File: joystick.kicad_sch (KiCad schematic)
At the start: 17 parts, among them J3 DB9_Male, J4 DB9_Male, U5 TXB0106PWR, U6 MCP23S17

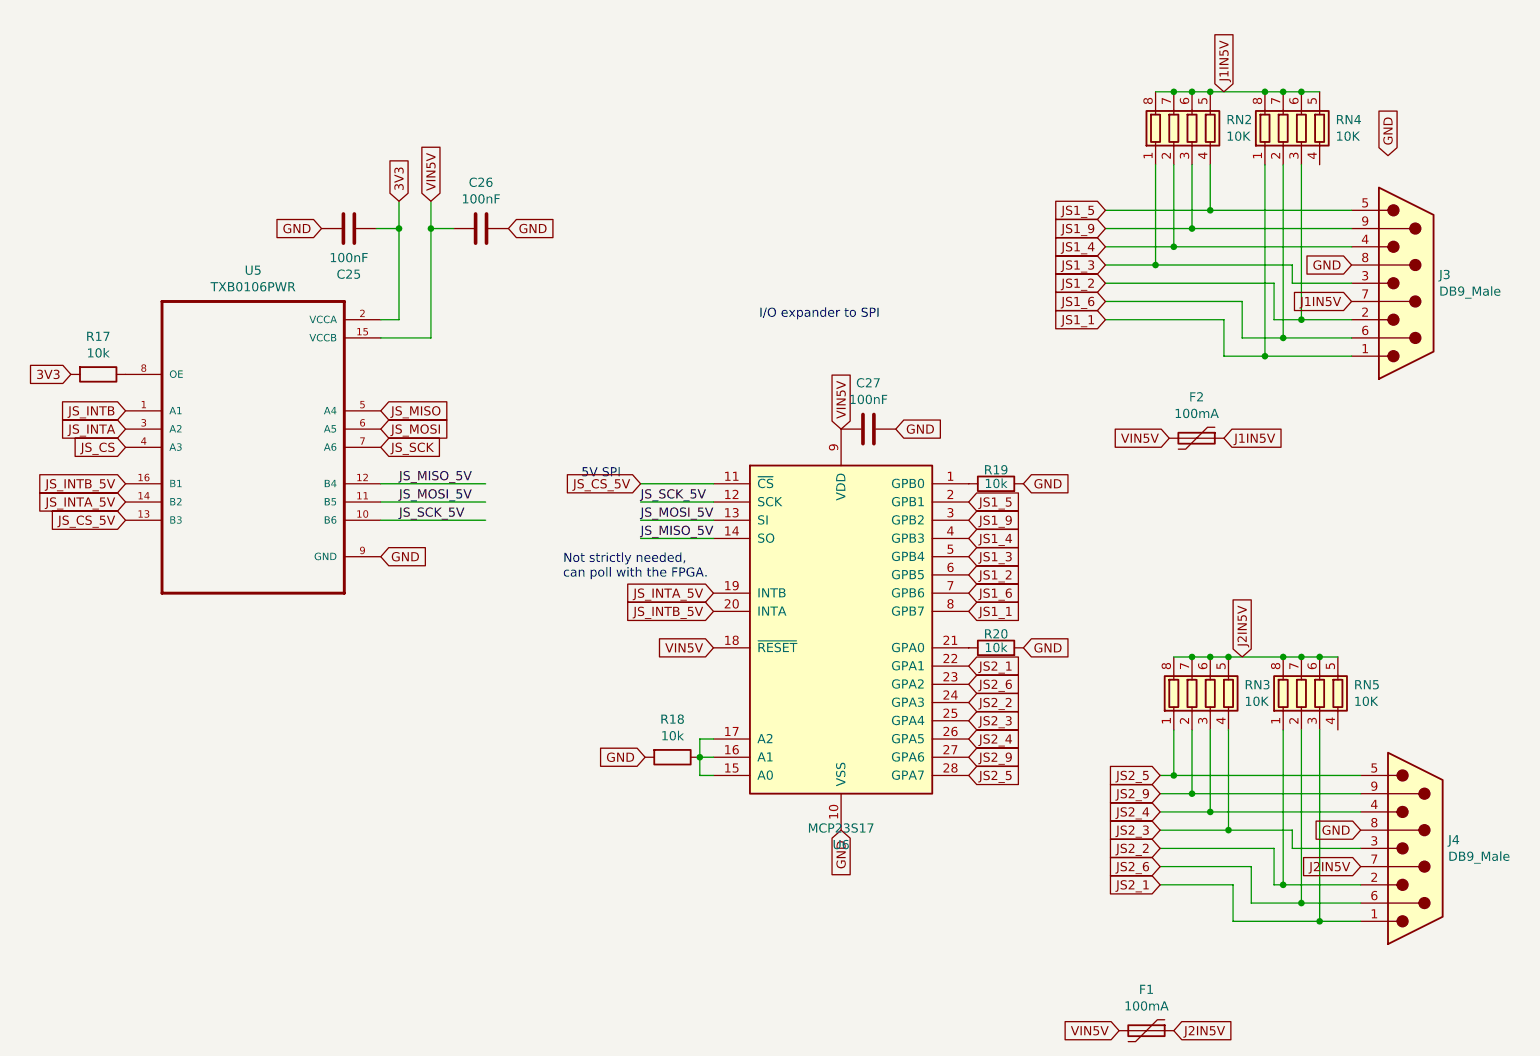
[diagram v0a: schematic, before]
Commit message: Prod version of OpenAARS 5.0 design.
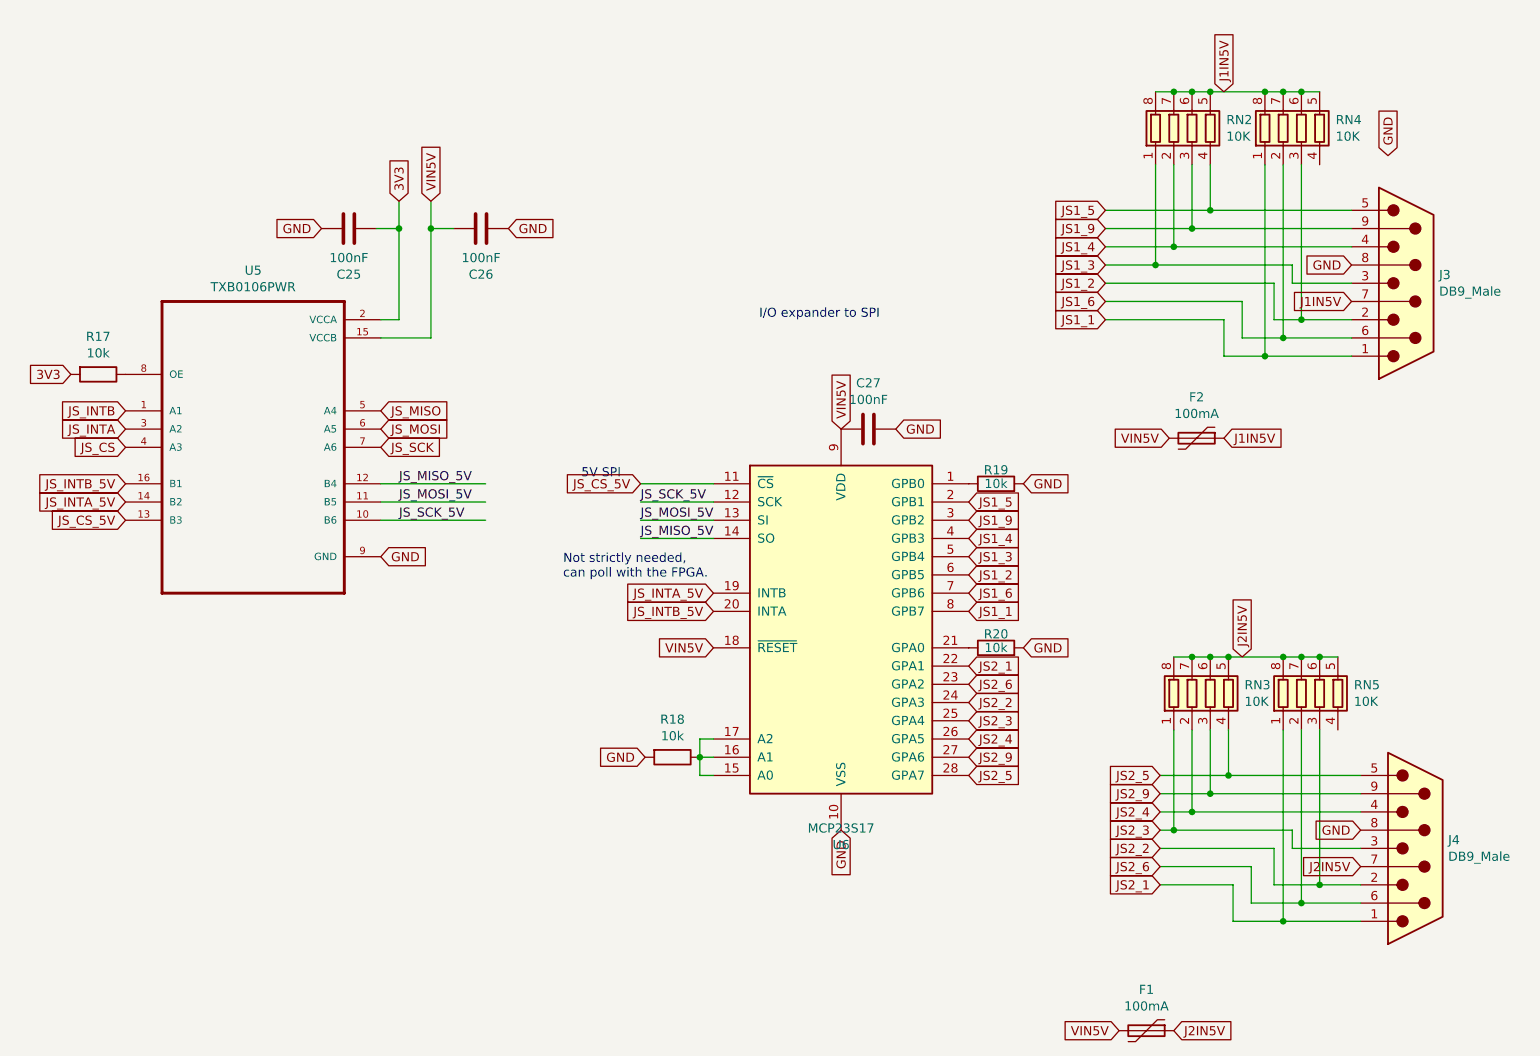
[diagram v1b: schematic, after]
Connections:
- net GND: now also C26.2; no longer C26.1
- net JS2_1: now also RN5.1 (R1.1); no longer RN5.3 (R3.1)
- net JS2_2: now also RN5.3 (R3.1); no longer RN5.1 (R1.1)
- net JS2_3: now also RN3.1 (R1.1); no longer RN3.4 (R4.1)
- net JS2_4: now also RN3.2 (R2.1); no longer RN3.3 (R3.1)
- net JS2_5: now also RN3.4 (R4.1); no longer RN3.1 (R1.1)
- net JS2_9: now also RN3.3 (R3.1); no longer RN3.2 (R2.1)
- net VIN5V: now also C26.1; no longer C26.2
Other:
- moved on the sheet: C26
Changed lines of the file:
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@@
   (junction (at 193.675 64.77) (diameter 0) (color 0 0 0 0)
   )
-  (junction (at 201.295 143.51) (diameter 0) (color 0 0 0 0)
-  )
   (junction (at 196.215 106.68) (diameter 0) (color 0 0 0 0)
   )
   (junction (at 201.295 106.68) (diameter 0) (color 0 0 0 0)
   )
-  (junction (at 180.975 123.19) (diameter 0) (color 0 0 0 0)
-  )
-  (junction (at 186.055 128.27) (diameter 0) (color 0 0 0 0)
-  )
   (junction (at 193.675 27.94) (diameter 0) (color 0 0 0 0)
   )
+  (junction (at 196.215 143.51) (diameter 0) (color 0 0 0 0)
+  )
   (junction (at 198.755 59.69) (diameter 0) (color 0 0 0 0)
   )
-  (junction (at 183.515 125.73) (diameter 0) (color 0 0 0 0)
-  )
   (junction (at 188.595 106.68) (diameter 0) (color 0 0 0 0)
   )
-  (junction (at 196.215 138.43) (diameter 0) (color 0 0 0 0)
-  )
   (junction (at 180.975 49.53) (diameter 0) (color 0 0 0 0)
   )
   (junction (at 180.975 27.94) (diameter 0) (color 0 0 0 0)
   )
+  (junction (at 186.055 125.73) (diameter 0) (color 0 0 0 0)
+  )
   (junction (at 73.025 46.99) (diameter 0) (color 0 0 0 0)
   )
+  (junction (at 188.595 123.19) (diameter 0) (color 0 0 0 0)
+  )
   (junction (at 186.055 44.45) (diameter 0) (color 0 0 0 0)
   )
@@
   (junction (at 186.055 106.68) (diameter 0) (color 0 0 0 0)
   )
+  (junction (at 201.295 138.43) (diameter 0) (color 0 0 0 0)
+  )
   (junction (at 196.215 62.23) (diameter 0) (color 0 0 0 0)
   )
@@
   (junction (at 183.515 106.68) (diameter 0) (color 0 0 0 0)
   )
+  (junction (at 183.515 128.27) (diameter 0) (color 0 0 0 0)
+  )
   (junction (at 198.755 27.94) (diameter 0) (color 0 0 0 0)
   )
@@
   (junction (at 183.515 27.94) (diameter 0) (color 0 0 0 0)
   )
-  (junction (at 188.595 130.81) (diameter 0) (color 0 0 0 0)
+  (junction (at 180.975 130.81) (diameter 0) (color 0 0 0 0)
   )
   (junction (at 114.935 120.65) (diameter 0) (color 0 0 0 0)
@@
     (stroke (width 0) (type default))
   )
-  (wire (pts (xy 188.595 130.81) (xy 197.485 130.81))
+  (wire (pts (xy 180.975 130.81) (xy 197.485 130.81))
     (stroke (width 0) (type default))
   )
@@
     (stroke (width 0) (type default))
   )
-  (wire (pts (xy 201.295 116.84) (xy 201.295 143.51))
+  (wire (pts (xy 196.215 116.84) (xy 196.215 143.51))
     (stroke (width 0) (type default))
   )
@@
     (stroke (width 0) (type default))
   )
-  (wire (pts (xy 180.975 116.84) (xy 180.975 123.19))
+  (wire (pts (xy 188.595 116.84) (xy 188.595 123.19))
     (stroke (width 0) (type default))
   )
@@
     (stroke (width 0) (type default))
   )
-  (wire (pts (xy 188.595 116.84) (xy 188.595 130.81))
-    (stroke (width 0) (type default))
-  )
   (wire (pts (xy 183.515 106.68) (xy 186.055 106.68))
     (stroke (width 0) (type default))
@@
     (stroke (width 0) (type default))
   )
-  (wire (pts (xy 194.945 138.43) (xy 196.215 138.43))
-    (stroke (width 0) (type default))
-  )
-  (wire (pts (xy 189.23 143.51) (xy 201.295 143.51))
-    (stroke (width 0) (type default))
-  )
-  (wire (pts (xy 179.07 123.19) (xy 180.975 123.19))
+  (wire (pts (xy 194.945 138.43) (xy 201.295 138.43))
+    (stroke (width 0) (type default))
+  )
+  (wire (pts (xy 189.23 143.51) (xy 196.215 143.51))
+    (stroke (width 0) (type default))
+  )
+  (wire (pts (xy 179.07 123.19) (xy 188.595 123.19))
     (stroke (width 0) (type default))
   )
@@
     (stroke (width 0) (type default))
   )
-  (wire (pts (xy 186.055 128.27) (xy 207.01 128.27))
-    (stroke (width 0) (type default))
-  )
   (wire (pts (xy 198.755 116.84) (xy 198.755 140.97))
     (stroke (width 0) (type default))
@@
     (stroke (width 0) (type default))
   )
-  (wire (pts (xy 179.07 128.27) (xy 186.055 128.27))
+  (wire (pts (xy 179.07 128.27) (xy 183.515 128.27))
     (stroke (width 0) (type default))
   )
@@
     (stroke (width 0) (type default))
   )
+  (wire (pts (xy 180.975 116.84) (xy 180.975 130.81))
+    (stroke (width 0) (type default))
+  )
+  (wire (pts (xy 186.055 125.73) (xy 207.01 125.73))
+    (stroke (width 0) (type default))
+  )
   (wire (pts (xy 171.45 57.15) (xy 190.5 57.15))
     (stroke (width 0) (type default))
@@
     (stroke (width 0) (type default))
   )
-  (wire (pts (xy 186.055 116.84) (xy 186.055 128.27))
-    (stroke (width 0) (type default))
-  )
   (wire (pts (xy 183.515 27.94) (xy 186.055 27.94))
     (stroke (width 0) (type default))
@@
     (stroke (width 0) (type default))
   )
-  (wire (pts (xy 179.07 130.81) (xy 188.595 130.81))
-    (stroke (width 0) (type default))
-  )
-  (wire (pts (xy 179.07 125.73) (xy 183.515 125.73))
+  (wire (pts (xy 179.07 130.81) (xy 180.975 130.81))
     (stroke (width 0) (type default))
   )
@@
     (stroke (width 0) (type default))
   )
-  (wire (pts (xy 201.295 143.51) (xy 207.01 143.51))
+  (wire (pts (xy 183.515 128.27) (xy 207.01 128.27))
     (stroke (width 0) (type default))
   )
@@
     (stroke (width 0) (type default))
   )
-  (wire (pts (xy 180.975 123.19) (xy 207.01 123.19))
-    (stroke (width 0) (type default))
-  )
   (wire (pts (xy 196.215 106.68) (xy 198.755 106.68))
     (stroke (width 0) (type default))
@@
     (stroke (width 0) (type default))
   )
-  (wire (pts (xy 196.215 116.84) (xy 196.215 138.43))
+  (wire (pts (xy 201.295 138.43) (xy 207.01 138.43))
+    (stroke (width 0) (type default))
+  )
+  (wire (pts (xy 183.515 116.84) (xy 183.515 128.27))
+    (stroke (width 0) (type default))
+  )
+  (wire (pts (xy 201.295 116.84) (xy 201.295 138.43))
     (stroke (width 0) (type default))
   )
@@
     (stroke (width 0) (type default))
   )
-  (wire (pts (xy 196.215 138.43) (xy 207.01 138.43))
-    (stroke (width 0) (type default))
-  )
   (wire (pts (xy 191.77 135.89) (xy 191.77 140.97))
     (stroke (width 0) (type default))
@@
     (stroke (width 0) (type default))
   )
-  (wire (pts (xy 183.515 125.73) (xy 207.01 125.73))
+  (wire (pts (xy 196.215 143.51) (xy 207.01 143.51))
+    (stroke (width 0) (type default))
+  )
+  (wire (pts (xy 188.595 123.19) (xy 207.01 123.19))
+    (stroke (width 0) (type default))
+  )
+  (wire (pts (xy 179.07 125.73) (xy 186.055 125.73))
     (stroke (width 0) (type default))
   )
@@
     (stroke (width 0) (type default))
   )
-  (wire (pts (xy 183.515 116.84) (xy 183.515 125.73))
+  (wire (pts (xy 186.055 116.84) (xy 186.055 125.73))
     (stroke (width 0) (type default))
   )
@@
     )
   )
-  (symbol (lib_id "Device:C") (at 84.455 46.99 270) (unit 1)
+  (symbol (lib_id "Device:C") (at 84.455 46.99 90) (unit 1)
     (in_bom yes) (on_board yes) (dnp no)
-    (property "Reference" "C26" (at 84.455 40.5892 90)
-      (effects (font (size 1.27 1.27)))
-    )
-    (property "Value" "100nF" (at 84.455 42.9006 90)
-      (effects (font (size 1.27 1.27)))
-    )
-    (property "Footprint" "Capacitor_SMD:C_0603_1608Metric" (at 80.645 47.9552 0)
-      (effects (font (size 1.27 1.27)) hide)
-    )
+    (property "Reference" "C26" (at 84.455 53.3908 90)
+      (effects (font (size 1.27 1.27)))
+    )
+    (property "Value" "100nF" (at 84.455 51.0794 90)
+      (effects (font (size 1.27 1.27)))
+    )
+    (property "Footprint" "Capacitor_SMD:C_0603_1608Metric" (at 88.265 46.0248 0)
+      (effects (font (size 1.27 1.27)) hide)
+    )
